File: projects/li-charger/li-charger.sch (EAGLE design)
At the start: 24 parts, among them J1 Power Jack, Q1 IRF5305, Q2 BC547, U1 7805, U2 Arduino Pro Mini

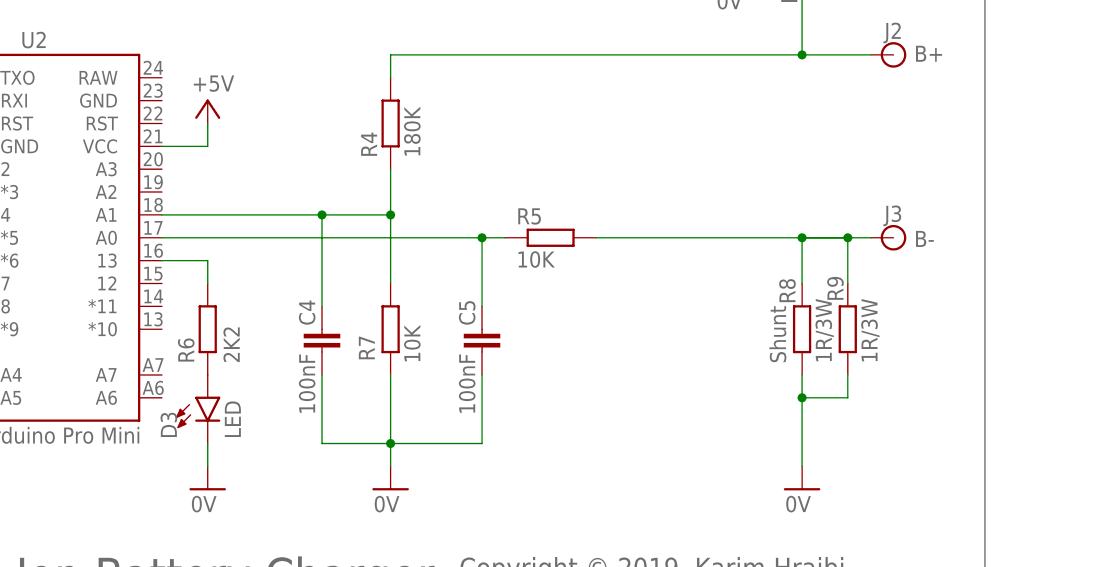
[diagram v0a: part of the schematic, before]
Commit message: Updated li-charger.sch
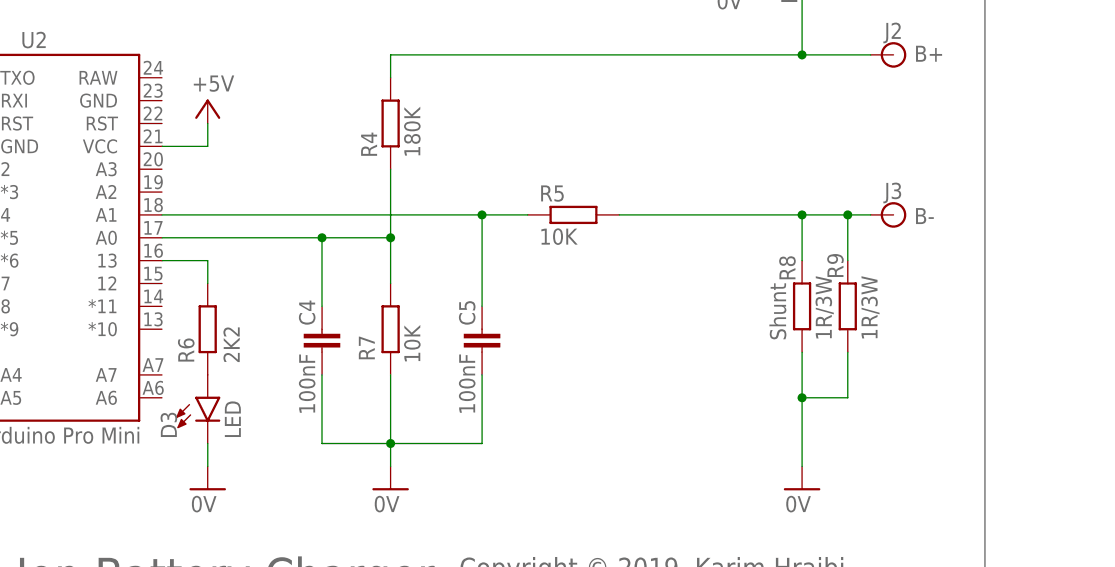
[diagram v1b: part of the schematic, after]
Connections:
- net N$10: now also U2.A0; no longer U2.A1
- net N$13: now also U2.A1; no longer U2.A0
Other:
- moved on the sheet: J3, R5, R8, R9
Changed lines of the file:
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@@
 www.microfarad.de/li-charger
 www.github.com/microfarad-de/li-charger</text>
-<text x="56.642" y="13.97" size="1.778" layer="95" rot="R90">Shunt</text>
+<text x="56.642" y="16.51" size="1.778" layer="95" rot="R90">Shunt</text>
 </plain>
 <instances>
@@
 <attribute name="VALUE" x="67.564" y="45.212" size="1.778" layer="96" font="vector"/>
 </instance>
-<instance part="J3" gate="G$1" x="68.58" y="27.94" smashed="yes">
-<attribute name="NAME" x="67.564" y="29.718" size="1.778" layer="95"/>
-<attribute name="VALUE" x="67.564" y="24.892" size="1.778" layer="96" font="vector"/>
+<instance part="J3" gate="G$1" x="68.58" y="30.48" smashed="yes">
+<attribute name="NAME" x="67.564" y="32.258" size="1.778" layer="95"/>
+<attribute name="VALUE" x="67.564" y="27.432" size="1.778" layer="96" font="vector"/>
 </instance>
 <instance part="J1" gate="G$1" x="-38.1" y="73.66" smashed="yes">
@@
 <attribute name="NAME" x="-48.26" y="73.66" size="1.778" layer="95"/>
 </instance>
-<instance part="R8" gate="G$1" x="58.42" y="17.78" smashed="yes" rot="R90">
-<attribute name="NAME" x="57.6834" y="20.574" size="1.778" layer="95" rot="R90"/>
-<attribute name="VALUE" x="61.722" y="13.97" size="1.778" layer="96" rot="R90"/>
+<instance part="R8" gate="G$1" x="58.42" y="20.32" smashed="yes" rot="R90">
+<attribute name="NAME" x="57.6834" y="23.114" size="1.778" layer="95" rot="R90"/>
+<attribute name="VALUE" x="61.722" y="16.51" size="1.778" layer="96" rot="R90"/>
 </instance>
 <instance part="C3" gate="G$1" x="12.7" y="76.2" smashed="yes">
@@
 <attribute name="VALUE" x="10.795" y="-2.54" size="1.778" layer="96"/>
 </instance>
-<instance part="R5" gate="G$1" x="30.48" y="27.94" smashed="yes">
-<attribute name="NAME" x="26.67" y="29.4386" size="1.778" layer="95"/>
-<attribute name="VALUE" x="26.67" y="24.638" size="1.778" layer="96"/>
+<instance part="R5" gate="G$1" x="33.02" y="30.48" smashed="yes">
+<attribute name="NAME" x="29.21" y="31.9786" size="1.778" layer="95"/>
+<attribute name="VALUE" x="29.21" y="27.178" size="1.778" layer="96"/>
 </instance>
 <instance part="D3" gate="G$1" x="-7.62" y="10.16" smashed="yes">
@@
 <attribute name="VALUE" x="-21.209" y="66.2686" size="1.778" layer="96" rot="R90"/>
 </instance>
-<instance part="R9" gate="G$1" x="63.5" y="17.78" smashed="yes" rot="R90">
-<attribute name="NAME" x="63.0174" y="20.828" size="1.778" layer="95" rot="R90"/>
-<attribute name="VALUE" x="66.802" y="13.97" size="1.778" layer="96" rot="R90"/>
+<instance part="R9" gate="G$1" x="63.5" y="20.32" smashed="yes" rot="R90">
+<attribute name="NAME" x="63.0174" y="23.368" size="1.778" layer="95" rot="R90"/>
+<attribute name="VALUE" x="66.802" y="16.51" size="1.778" layer="96" rot="R90"/>
 </instance>
 <instance part="D2" gate="1" x="58.42" y="63.5" smashed="yes" rot="R270">
@@
 <pinref part="R8" gate="G$1" pin="1"/>
 <wire x1="58.42" y1="10.16" x2="63.5" y2="10.16" width="0.1524" layer="91"/>
-<wire x1="63.5" y1="10.16" x2="63.5" y2="12.7" width="0.1524" layer="91"/>
-<wire x1="58.42" y1="12.7" x2="58.42" y2="10.16" width="0.1524" layer="91"/>
+<wire x1="63.5" y1="10.16" x2="63.5" y2="15.24" width="0.1524" layer="91"/>
+<wire x1="58.42" y1="15.24" x2="58.42" y2="10.16" width="0.1524" layer="91"/>
 <junction x="58.42" y="10.16"/>
 </segment>
@@
 </segment>
 </net>
-<net name="B-" class="0">
-<segment>
-<pinref part="J3" gate="G$1" pin="1"/>
-<pinref part="R5" gate="G$1" pin="2"/>
-<wire x1="35.56" y1="27.94" x2="58.42" y2="27.94" width="0.1524" layer="91"/>
-<label x="70.866" y="26.924" size="1.778" layer="95"/>
-<pinref part="R8" gate="G$1" pin="2"/>
-<wire x1="58.42" y1="27.94" x2="63.5" y2="27.94" width="0.1524" layer="91"/>
-<wire x1="63.5" y1="27.94" x2="66.04" y2="27.94" width="0.1524" layer="91"/>
-<wire x1="58.42" y1="22.86" x2="58.42" y2="27.94" width="0.1524" layer="91"/>
-<junction x="58.42" y="27.94"/>
-<pinref part="R9" gate="G$1" pin="2"/>
-<wire x1="63.5" y1="22.86" x2="63.5" y2="27.94" width="0.1524" layer="91"/>
-<junction x="63.5" y="27.94"/>
-</segment>
-</net>
 <net name="B+" class="0">
 <segment>
@@
 <net name="N$10" class="0">
 <segment>
-<pinref part="U2" gate="G$1" pin="A1"/>
 <pinref part="R4" gate="G$1" pin="1"/>
-<wire x1="-12.7" y1="30.48" x2="5.08" y2="30.48" width="0.1524" layer="91"/>
-<wire x1="5.08" y1="30.48" x2="12.7" y2="30.48" width="0.1524" layer="91"/>
-<wire x1="12.7" y1="30.48" x2="12.7" y2="35.56" width="0.1524" layer="91"/>
-<wire x1="5.08" y1="20.32" x2="5.08" y2="30.48" width="0.1524" layer="91"/>
-<junction x="5.08" y="30.48"/>
+<wire x1="5.08" y1="27.94" x2="12.7" y2="27.94" width="0.1524" layer="91"/>
+<wire x1="12.7" y1="27.94" x2="12.7" y2="35.56" width="0.1524" layer="91"/>
+<wire x1="5.08" y1="20.32" x2="5.08" y2="27.94" width="0.1524" layer="91"/>
 <pinref part="R7" gate="G$1" pin="2"/>
-<wire x1="12.7" y1="22.86" x2="12.7" y2="30.48" width="0.1524" layer="91"/>
-<junction x="12.7" y="30.48"/>
+<wire x1="12.7" y1="22.86" x2="12.7" y2="27.94" width="0.1524" layer="91"/>
+<junction x="12.7" y="27.94"/>
 <pinref part="C4" gate="G$1" pin="1"/>
+<pinref part="U2" gate="G$1" pin="A0"/>
+<wire x1="5.08" y1="27.94" x2="-12.7" y2="27.94" width="0.1524" layer="91"/>
+<junction x="5.08" y="27.94"/>
 </segment>
 </net>
@@
 <segment>
 <pinref part="R5" gate="G$1" pin="1"/>
-<wire x1="25.4" y1="27.94" x2="22.86" y2="27.94" width="0.1524" layer="91"/>
-<pinref part="U2" gate="G$1" pin="A0"/>
-<wire x1="22.86" y1="27.94" x2="-12.7" y2="27.94" width="0.1524" layer="91"/>
-<wire x1="22.86" y1="20.32" x2="22.86" y2="27.94" width="0.1524" layer="91"/>
-<junction x="22.86" y="27.94"/>
+<wire x1="27.94" y1="30.48" x2="22.86" y2="30.48" width="0.1524" layer="91"/>
+<wire x1="22.86" y1="20.32" x2="22.86" y2="30.48" width="0.1524" layer="91"/>
 <pinref part="C5" gate="G$1" pin="1"/>
+<pinref part="U2" gate="G$1" pin="A1"/>
+<wire x1="22.86" y1="30.48" x2="-12.7" y2="30.48" width="0.1524" layer="91"/>
+<junction x="22.86" y="30.48"/>
 </segment>
 </net>
@@
 </segment>
 </net>
-<net name="N$7" class="0">
-<segment>
-<wire x1="63.5" y1="27.94" x2="58.42" y2="27.94" width="0.1524" layer="91"/>
-</segment>
-</net>
+<net name="B-" class="0">
+<segment>
+<pinref part="J3" gate="G$1" pin="1"/>
+<pinref part="R5" gate="G$1" pin="2"/>
+<wire x1="38.1" y1="30.48" x2="58.42" y2="30.48" width="0.1524" layer="91"/>
+<label x="70.866" y="29.464" size="1.778" layer="95"/>
+<pinref part="R8" gate="G$1" pin="2"/>
+<wire x1="58.42" y1="30.48" x2="63.5" y2="30.48" width="0.1524" layer="91"/>
+<wire x1="63.5" y1="30.48" x2="66.04" y2="30.48" width="0.1524" layer="91"/>
+<wire x1="58.42" y1="25.4" x2="58.42" y2="30.48" width="0.1524" layer="91"/>
+<junction x="58.42" y="30.48"/>
+<pinref part="R9" gate="G$1" pin="2"/>
+<wire x1="63.5" y1="25.4" x2="63.5" y2="30.48" width="0.1524" layer="91"/>
+<junction x="63.5" y="30.48"/>
+</segment>
+</net>
